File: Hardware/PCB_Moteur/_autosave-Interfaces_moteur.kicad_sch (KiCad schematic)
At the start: 27 parts, among them J3 Conn_01x02, J7 Conn_02x06_Top_Bottom, U12 MCP1802T-5002I/OT, U2 ISOW1044, U4 LSF0204PWR

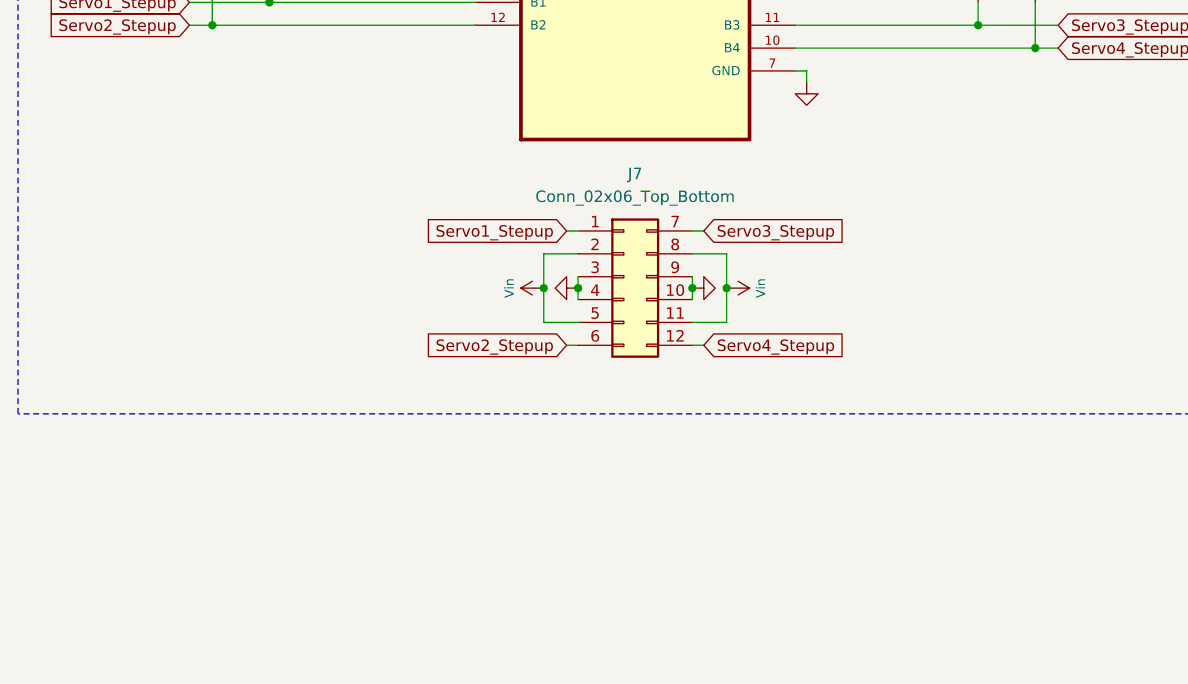
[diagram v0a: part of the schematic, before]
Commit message: fix: minor corrections aux servos avant souper
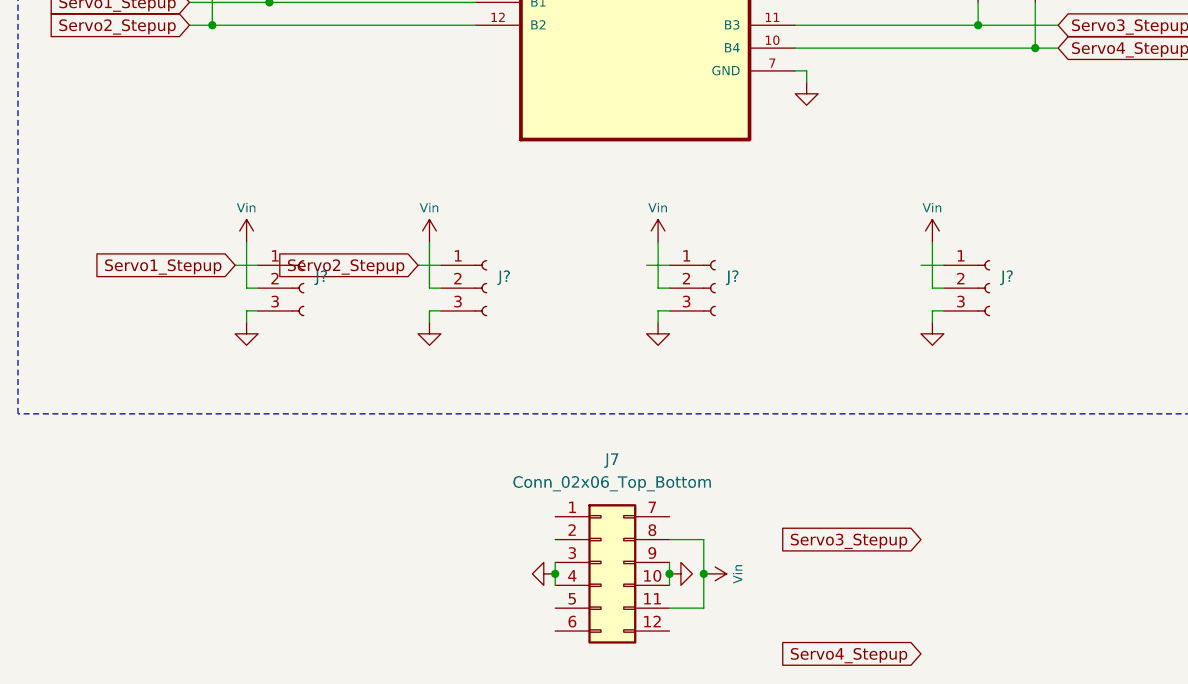
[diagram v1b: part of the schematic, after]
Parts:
- added J? (x4): Conn_01x03_Socket, symbol Connector:Conn_01x03_Socket
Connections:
- net GND: now also J?.3 (Pin_3), J?.3 (Pin_3), J?.3 (Pin_3), J?.3 (Pin_3)
- net Servo1_Stepup: now also J?.1 (Pin_1); no longer J7.1 (Pin_1)
- net Servo2_Stepup: now also J?.1 (Pin_1); no longer J7.6 (Pin_6)
- net Servo3_Stepup: no longer J7.7 (Pin_7)
- net Servo4_Stepup: no longer J7.12 (Pin_12)
- net Vin: now also J?.2 (Pin_2), J?.2 (Pin_2), J?.2 (Pin_2), J?.2 (Pin_2); no longer J7.2 (Pin_2), J7.5 (Pin_5)
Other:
- moved on the sheet: J7
